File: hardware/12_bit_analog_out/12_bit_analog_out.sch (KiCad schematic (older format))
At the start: 30 parts, among them J1 Inputs, J2 Outputs, U1 LM4040-10, U2 MCP4728, U3 OPA4197

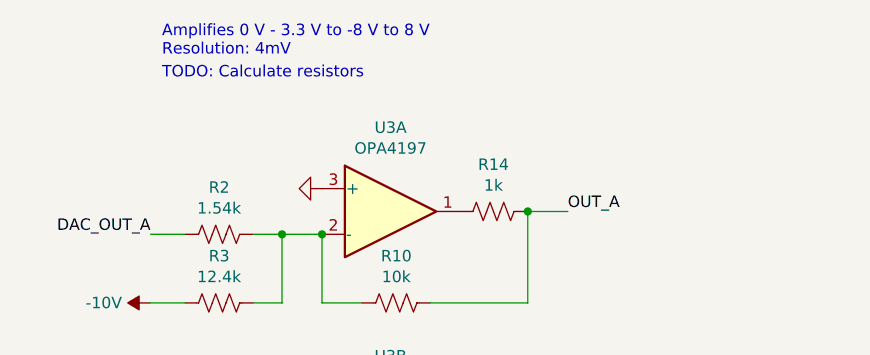
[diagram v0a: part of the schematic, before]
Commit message: Add note about range resistors
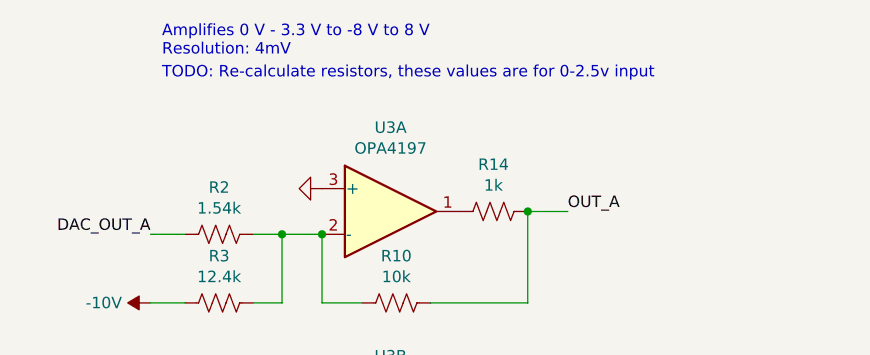
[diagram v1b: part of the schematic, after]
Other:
- note added: "TODO: Re-calculate resistors, these values are for 0-2.5v input\n"
- note removed: "TODO: Calculate resistors"
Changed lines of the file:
@@
 $EndComp
 Text Notes 7150 1425 0    50   ~ 0
-TODO: Calculate resistors
+TODO: Re-calculate resistors, these values are for 0-2.5v input\n
 Text Label 3850 5725 2    50   ~ 0
 ~LDAC
